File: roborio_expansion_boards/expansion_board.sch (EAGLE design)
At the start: 19 parts

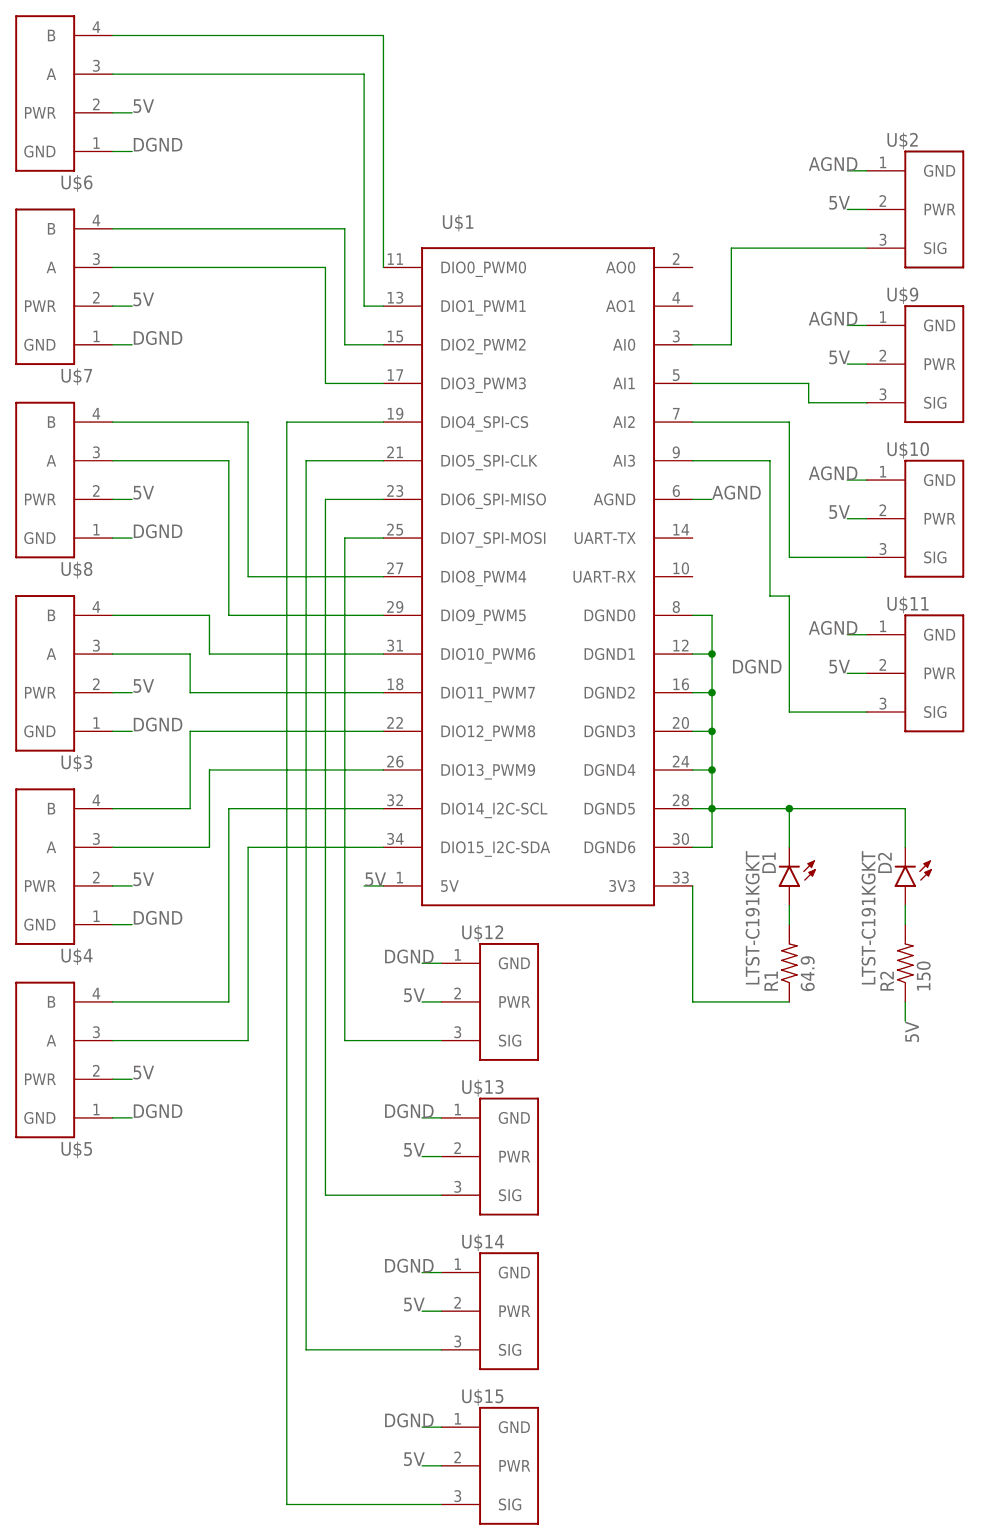
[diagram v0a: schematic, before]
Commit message: added capacitors to the power lines near each connector
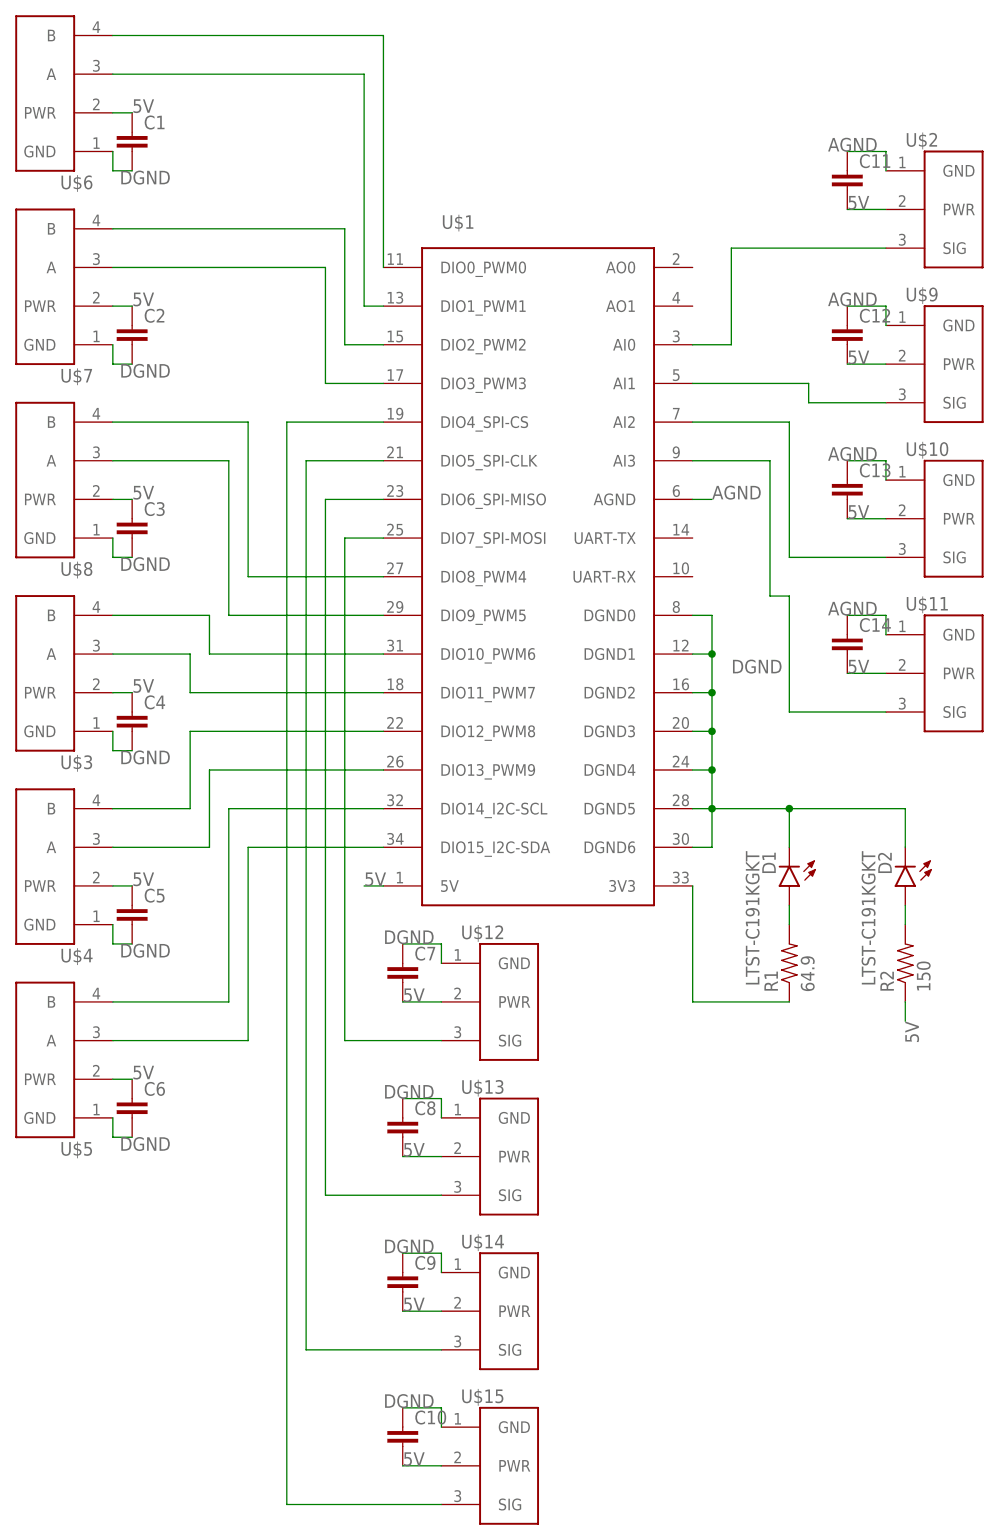
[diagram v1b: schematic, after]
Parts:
- added C1, C10, C11, C12, C13, C14, C2, C3, C4, C5, C6, C7, C8, C9: (no value), custom:CAP0603
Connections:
- net 5V: now also C1.1, C10.2, C11.2, C12.2, C13.2, C14.2, C2.1, C3.1, C4.1, C5.1, C6.1, C7.2, C8.2, C9.2
- net AGND: now also C11.1, C12.1, C13.1, C14.1
- net DGND: now also C1.2, C10.1, C2.2, C3.2, C4.2, C5.2, C6.2, C7.1, C8.1, C9.1
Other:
- moved on the sheet: U$10, U$11, U$2, U$9
